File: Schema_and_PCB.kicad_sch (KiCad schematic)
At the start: 0 parts

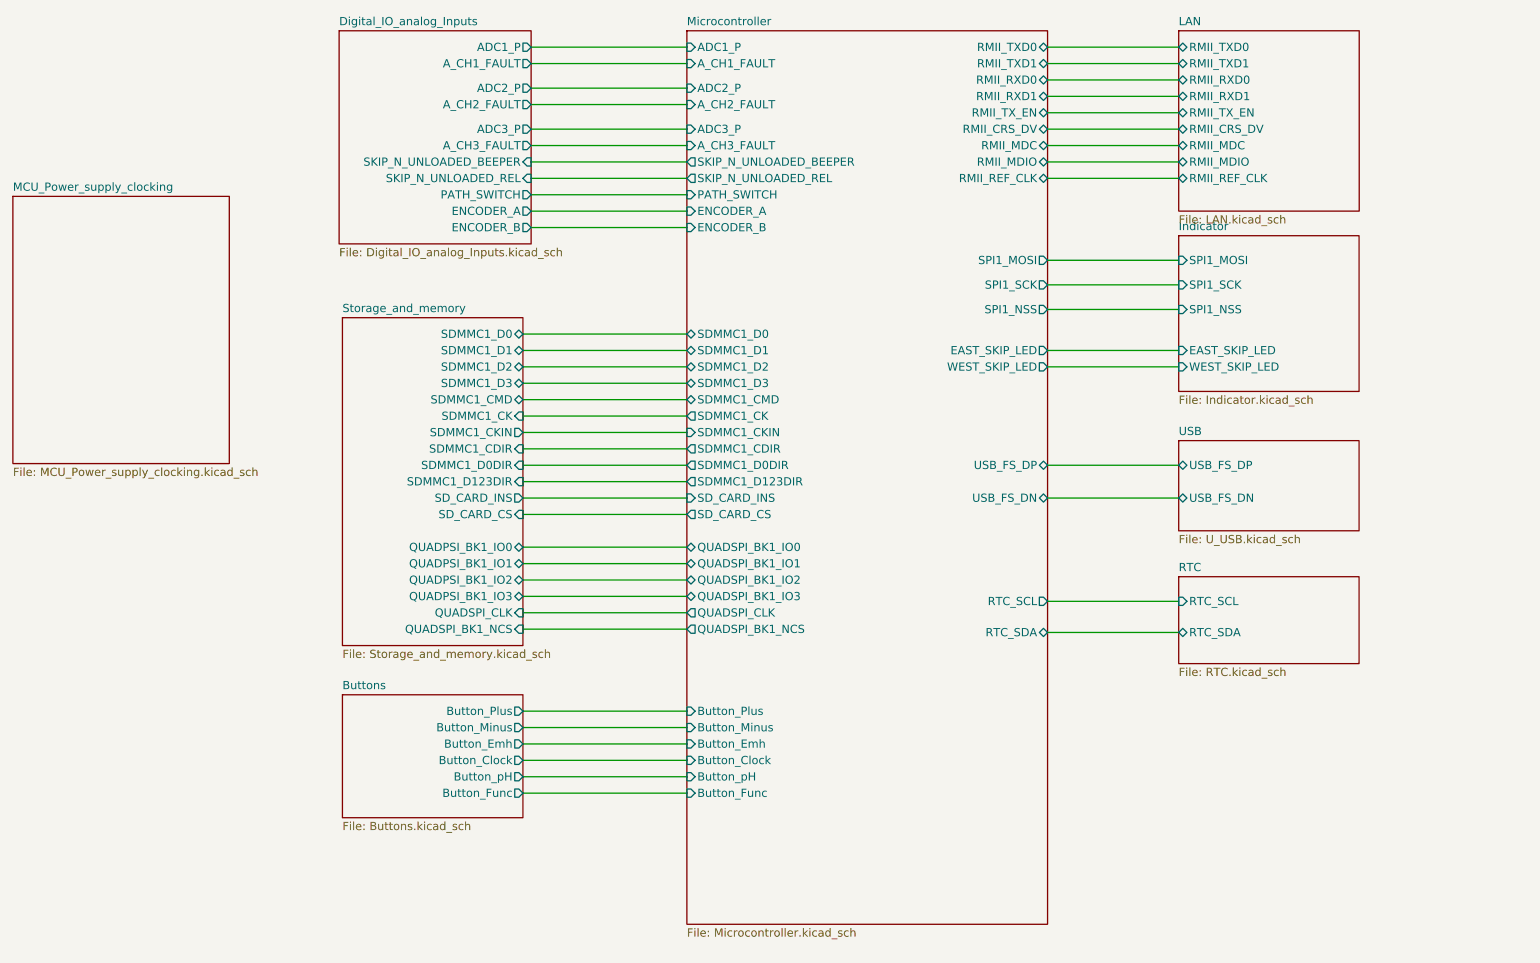
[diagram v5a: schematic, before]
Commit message: External connectors sheet added
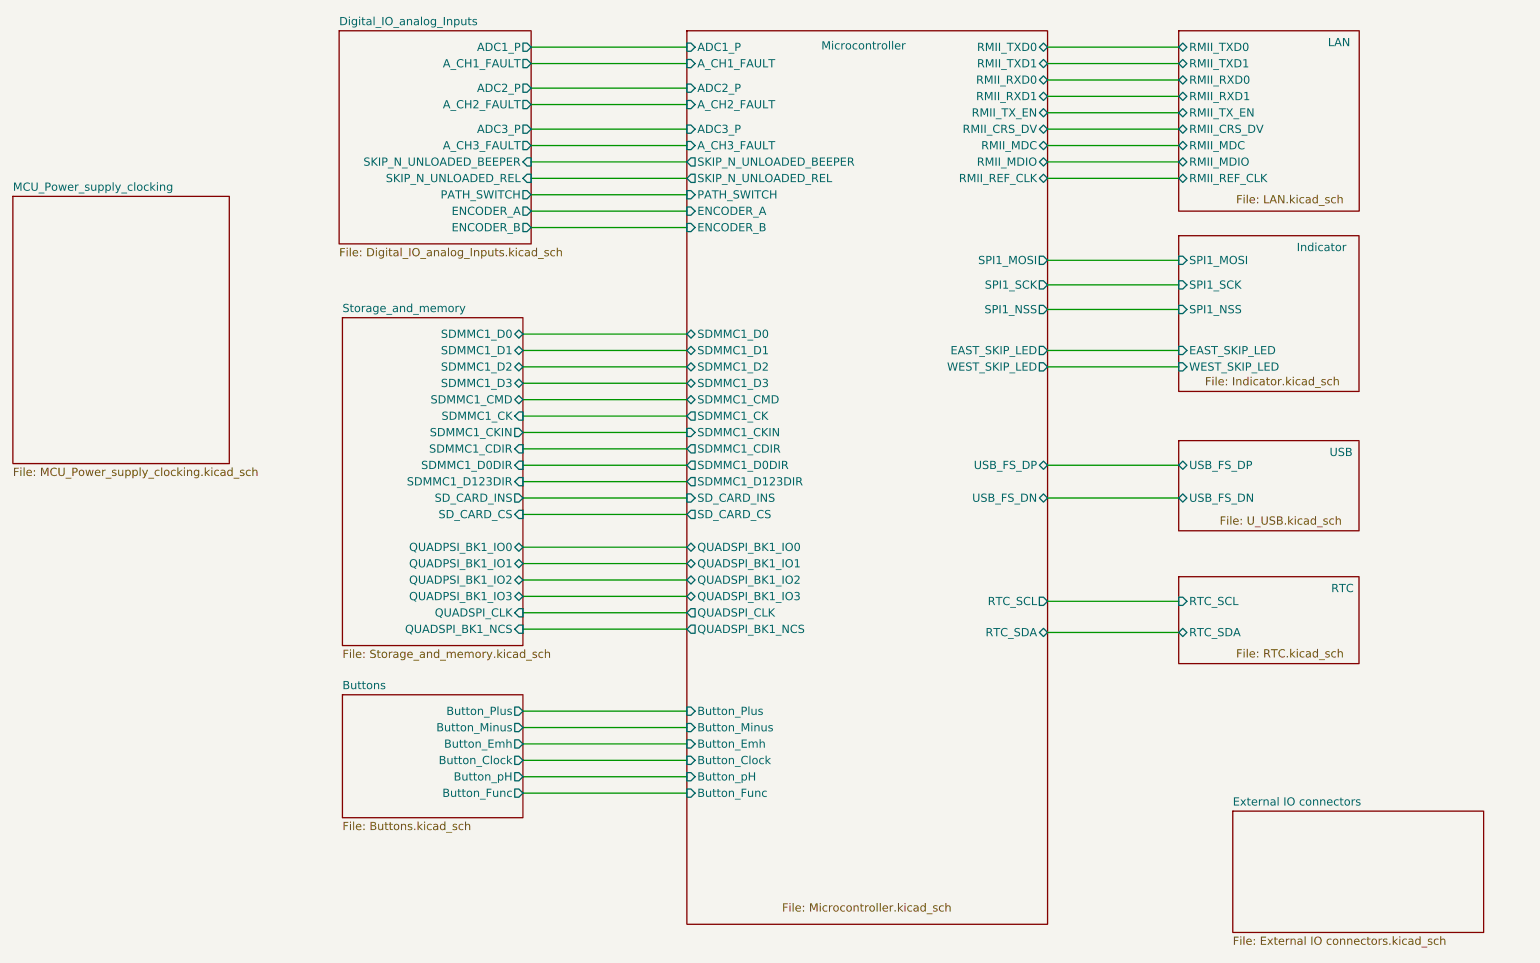
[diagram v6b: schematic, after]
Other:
- added sheet External IO connectors (External IO connectors.kicad_sch)
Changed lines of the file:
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@@
     (stroke (width 0) (type default) (color 0 0 0 0))
   )
-  (sheet (at 217.17 21.59) (size 27.9654 27.94) (fields_autoplaced)
+  (sheet (at 217.17 21.59) (size 27.9654 27.94)
     (stroke (width 0) (type solid) (color 0 0 0 0))
     (fill (color 0 0 0 0.0000))
-    (property "Sheet name" "LAN" (id 0) (at 217.17 20.8784 0)
+    (property "Sheet name" "LAN" (id 0) (at 240.284 24.13 0)
       (effects (font (size 1.27 1.27)) (justify left bottom))
     )
-    (property "Sheet file" "LAN.kicad_sch" (id 1) (at 217.17 50.1146 0)
+    (property "Sheet file" "LAN.kicad_sch" (id 1) (at 226.06 46.99 0)
       (effects (font (size 1.27 1.27)) (justify left top))
     )
@@
     )
   )
-  (sheet (at 217.17 53.34) (size 27.94 24.13) (fields_autoplaced)
+  (sheet (at 217.17 53.34) (size 27.94 24.13)
     (stroke (width 0) (type solid) (color 0 0 0 0))
     (fill (color 0 0 0 0.0000))
-    (property "Sheet name" "Indicator" (id 0) (at 217.17 52.6284 0)
+    (property "Sheet name" "Indicator" (id 0) (at 235.458 55.88 0)
       (effects (font (size 1.27 1.27)) (justify left bottom))
     )
-    (property "Sheet file" "Indicator.kicad_sch" (id 1) (at 217.17 78.0546 0)
+    (property "Sheet file" "Indicator.kicad_sch" (id 1) (at 221.234 75.184 0)
       (effects (font (size 1.27 1.27)) (justify left top))
     )
@@
     )
   )
-  (sheet (at 217.17 85.09) (size 27.94 13.97) (fields_autoplaced)
+  (sheet (at 217.17 85.09) (size 27.94 13.97)
     (stroke (width 0) (type solid) (color 0 0 0 0))
     (fill (color 0 0 0 0.0000))
-    (property "Sheet name" "USB" (id 0) (at 217.17 84.3784 0)
+    (property "Sheet name" "USB" (id 0) (at 240.538 87.63 0)
       (effects (font (size 1.27 1.27)) (justify left bottom))
     )
-    (property "Sheet file" "U_USB.kicad_sch" (id 1) (at 217.17 99.6446 0)
+    (property "Sheet file" "U_USB.kicad_sch" (id 1) (at 223.52 96.774 0)
       (effects (font (size 1.27 1.27)) (justify left top))
     )
@@
     )
   )
-  (sheet (at 140.97 21.59) (size 55.88 138.43) (fields_autoplaced)
+  (sheet (at 140.97 21.59) (size 55.88 138.43)
     (stroke (width 0) (type solid) (color 0 0 0 0))
     (fill (color 0 0 0 0.0000))
-    (property "Sheet name" "Microcontroller" (id 0) (at 140.97 20.8784 0)
+    (property "Sheet name" "Microcontroller" (id 0) (at 161.798 24.638 0)
       (effects (font (size 1.27 1.27)) (justify left bottom))
     )
-    (property "Sheet file" "Microcontroller.kicad_sch" (id 1) (at 140.97 160.6046 0)
+    (property "Sheet file" "Microcontroller.kicad_sch" (id 1) (at 155.702 156.718 0)
       (effects (font (size 1.27 1.27)) (justify left top))
     )
@@
     )
   )
-  (sheet (at 217.17 106.172) (size 27.94 13.462) (fields_autoplaced)
+  (sheet (at 217.17 106.172) (size 27.94 13.462)
     (stroke (width 0) (type solid) (color 0 0 0 0))
     (fill (color 0 0 0 0.0000))
-    (property "Sheet name" "RTC" (id 0) (at 217.17 105.4604 0)
+    (property "Sheet name" "RTC" (id 0) (at 240.792 108.712 0)
       (effects (font (size 1.27 1.27)) (justify left bottom))
     )
-    (property "Sheet file" "RTC.kicad_sch" (id 1) (at 217.17 120.2186 0)
+    (property "Sheet file" "RTC.kicad_sch" (id 1) (at 226.06 117.348 0)
       (effects (font (size 1.27 1.27)) (justify left top))
     )
@@
     (pin "RTC_SDA" bidirectional (at 217.17 114.808 180)
       (effects (font (size 1.27 1.27)) (justify left))
+    )
+  )
+  (sheet (at 225.552 142.494) (size 38.862 18.796) (fields_autoplaced)
+    (stroke (width 0.1524) (type solid) (color 0 0 0 0))
+    (fill (color 0 0 0 0.0000))
+    (property "Sheet name" "External IO connectors" (id 0) (at 225.552 141.7824 0)
+      (effects (font (size 1.27 1.27)) (justify left bottom))
+    )
+    (property "Sheet file" "External IO connectors.kicad_sch" (id 1) (at 225.552 161.8746 0)
+      (effects (font (size 1.27 1.27)) (justify left top))
     )
   )
@@
     (path "/00000000-0000-0000-0000-00006099558b" (page "9"))
     (path "/00000000-0000-0000-0000-0000619a1dc2" (page "10"))
+    (path "/c5a6ee00-8c8f-47f9-b4bc-c68a1a04bf77" (page "11"))
   )
   (symbol_instances
@@
       (reference "U30") (unit 1) (value "LAN8742A-CZ-TR") (footprint "SVIELCOM:Microchip-C04-143B-S4QFN-0-0-IPC_A")
     )
+    (path "/c5a6ee00-8c8f-47f9-b4bc-c68a1a04bf77/3ce6848b-3c5c-4960-a4ef-6b07b0879983"
+      (reference "XS?") (unit 1) (value "2РМТ22Б10Ш1В1В") (footprint "")
+    )
+    (path "/c5a6ee00-8c8f-47f9-b4bc-c68a1a04bf77/c3d04406-a65c-41d7-bdc0-7ab6e616b2d1"
+      (reference "XS?") (unit 1) (value "2РМТ24Б19Ш1В1В") (footprint "")
+    )
     (path "/00000000-0000-0000-0000-000060a03f8a/00000000-0000-0000-0000-000060a2f6e4"
